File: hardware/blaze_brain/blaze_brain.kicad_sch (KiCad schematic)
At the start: 26 parts, among them J1 Conn_01x02, J2 Conn_01x02, J3 Conn_01x30, J4 Micro_SD_Card, J5 Conn_01x03_Pin, Q1 DMG2305UX, Q2 FDN340P, U1 AZ1117-5.0, U2 AZ1117-3.3, U3 Teensy4.0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

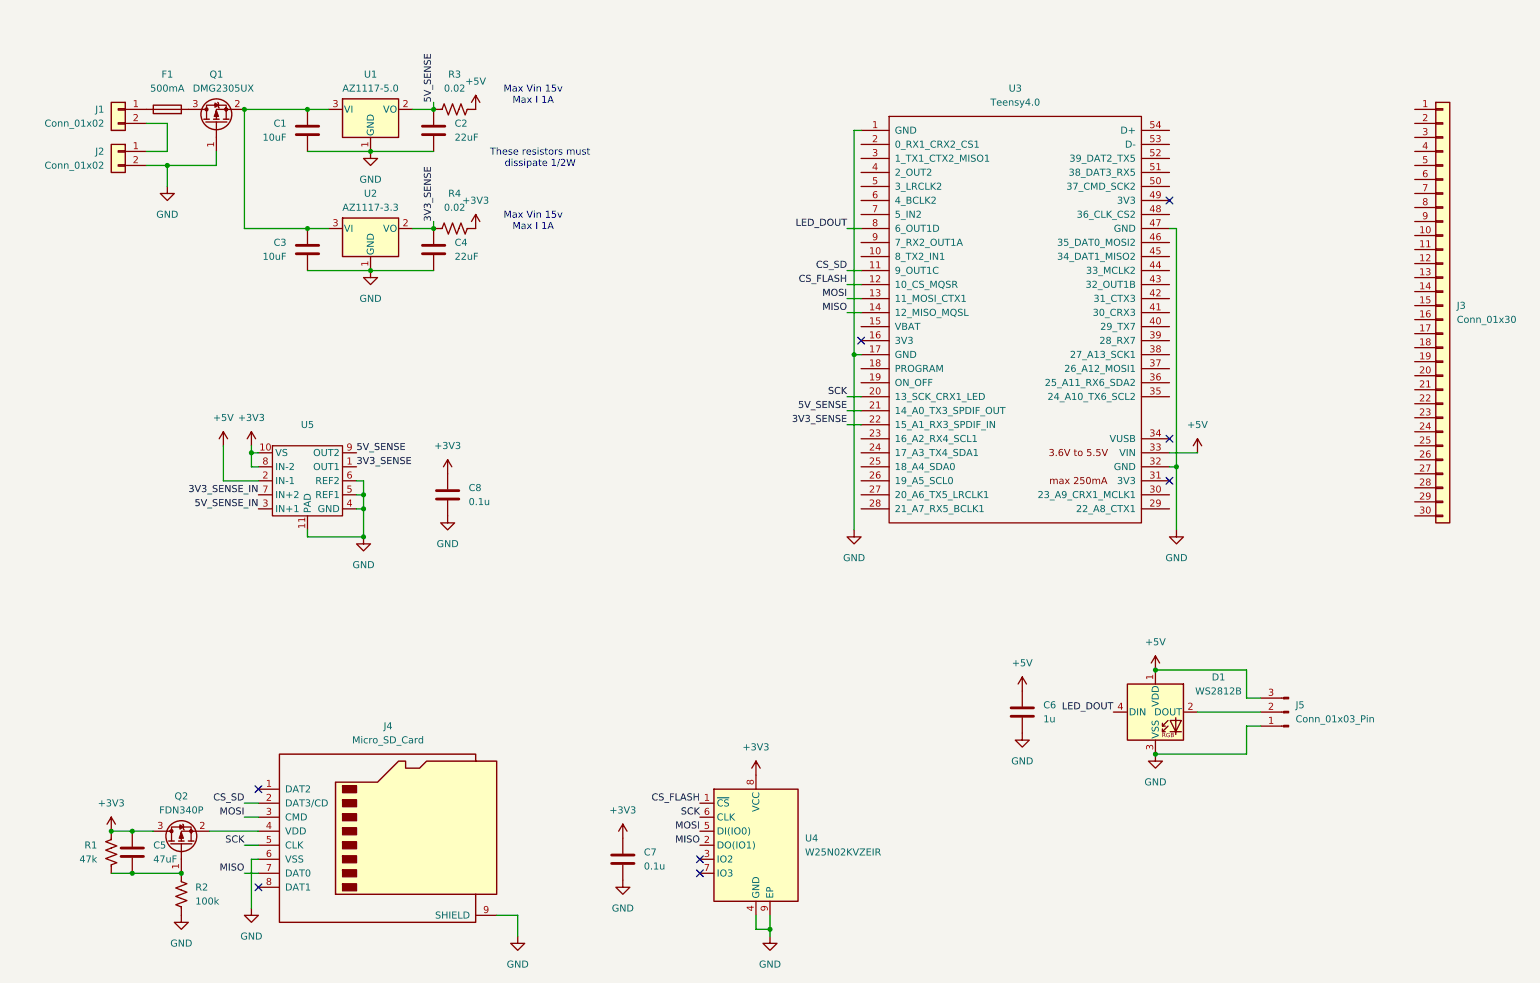
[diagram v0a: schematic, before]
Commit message: Moved main power function to power management
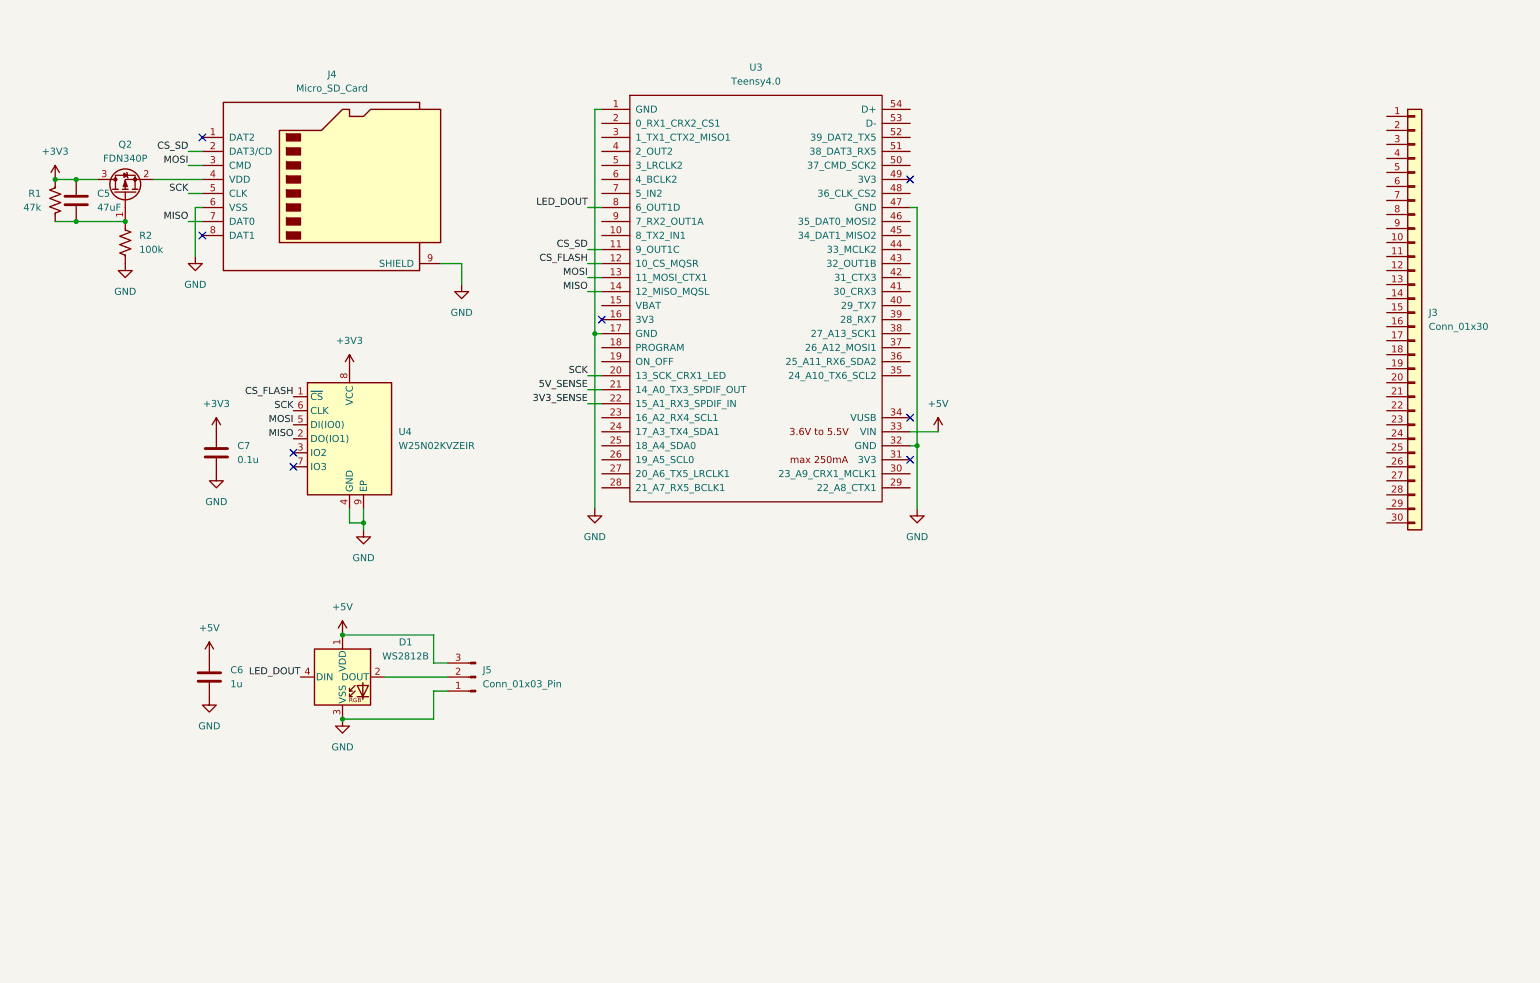
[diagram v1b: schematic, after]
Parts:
- removed C1, C3: 10uF, symbol Device:C
- removed C2, C4: 22uF, symbol Device:C
- removed C8: 0.1u, symbol Device:C
- removed F1: 500mA, symbol Device:Fuse
- removed J1, J2: Conn_01x02, symbol Connector_Generic:Conn_01x02
- removed Q1: DMG2305UX, Package_TO_SOT_SMD:SOT-23, symbol Transistor_FET:DMG2301L
- removed R3, R4: 0.02, symbol Device:R_US
- removed U1: AZ1117-5.0, Package_TO_SOT_SMD:SOT-223-3_TabPin2, symbol Regulator_Linear:AZ1117-5.0
- removed U2: AZ1117-3.3, Package_TO_SOT_SMD:SOT-223-3_TabPin2, symbol Regulator_Linear:AZ1117-5.0
- removed U5: ~, symbol Blaze_Lib:INA2181
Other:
- note removed: "Max Vin 15v Max I 1A"
- note removed: "These resistors must dissipate 1/2W"
- moved on the sheet: C5, C6, C7, D1, J3, J4, J5, Q2, R1, R2, U3, U4

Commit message: Created blaze sense, updated brain
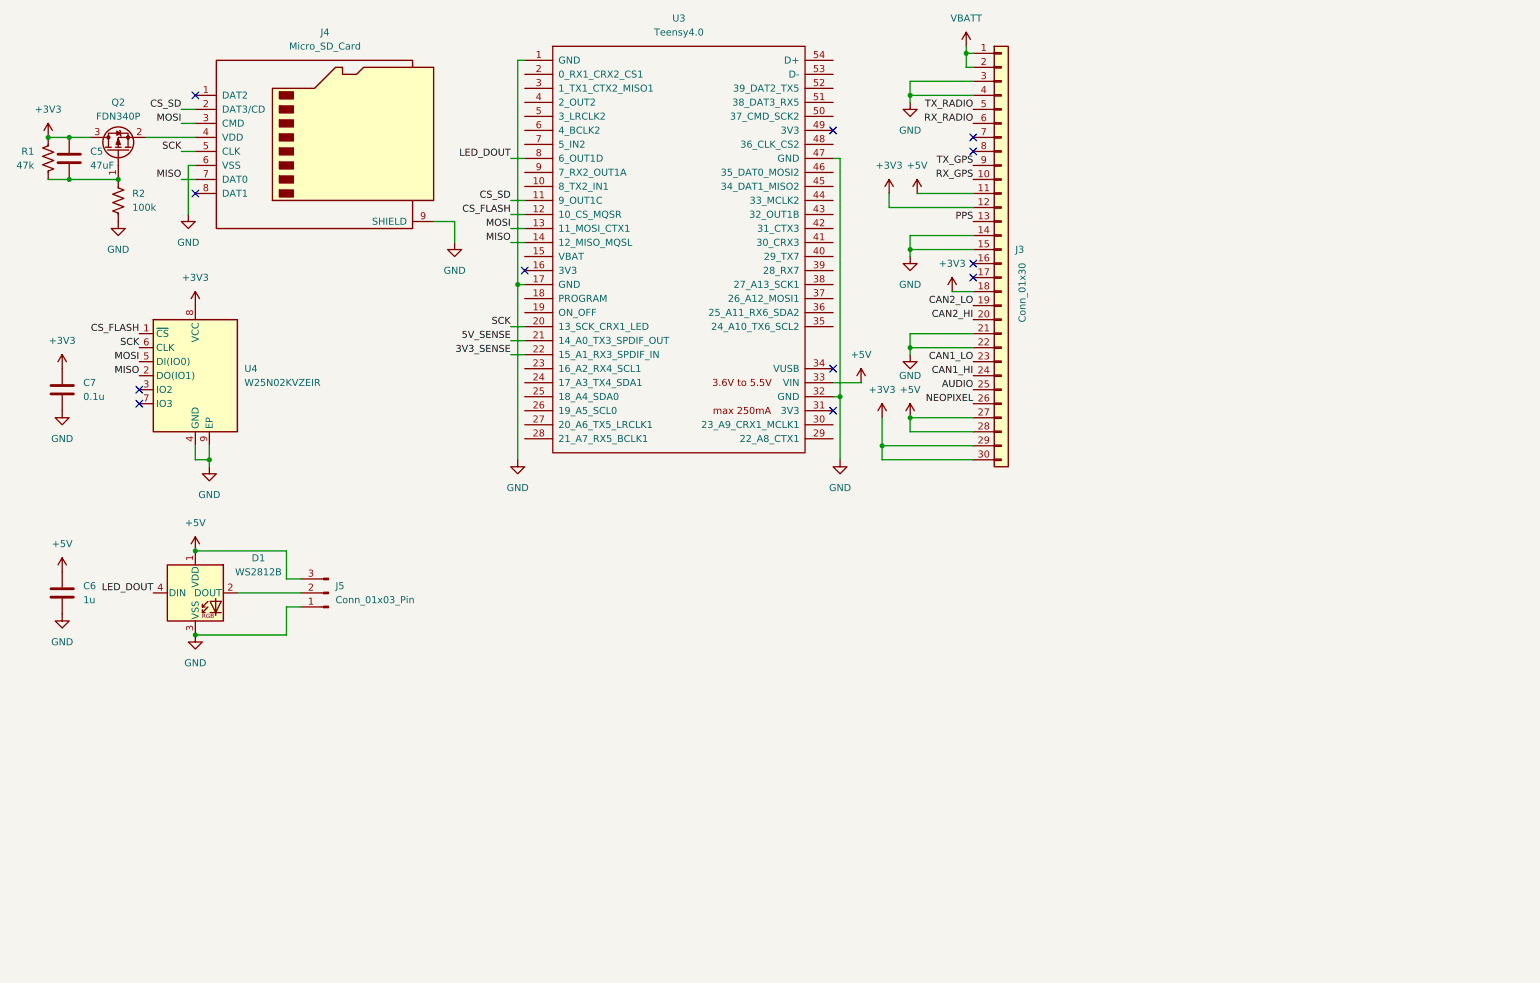
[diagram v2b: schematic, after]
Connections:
- net +3V3: now also J3.12 (Pin_12), J3.18 (Pin_18), J3.29 (Pin_29), J3.30 (Pin_30)
- net +5V: now also J3.11 (Pin_11), J3.27 (Pin_27), J3.28 (Pin_28)
- net GND: now also J3.14 (Pin_14), J3.15 (Pin_15), J3.21 (Pin_21), J3.22 (Pin_22), J3.3 (Pin_3), J3.4 (Pin_4)
- net VBATT: now reaches J3.1 (Pin_1)
- net VBATT: now also J3.2 (Pin_2)
- net RX_GPS: now reaches J3.10 (Pin_10)
- net PPS: now reaches J3.13 (Pin_13)
- net CAN2_LO: now reaches J3.19 (Pin_19)
- net CAN2_HI: now reaches J3.20 (Pin_20)
- net CAN1_LO: now reaches J3.23 (Pin_23)
- net CAN1_HI: now reaches J3.24 (Pin_24)
- net AUDIO: now reaches J3.25 (Pin_25)
- net NEOPIXEL: now reaches J3.26 (Pin_26)
- net TX_RADIO: now reaches J3.5 (Pin_5)
- net RX_RADIO: now reaches J3.6 (Pin_6)
- net TX_GPS: now reaches J3.9 (Pin_9)
- no-connect marks 8 -> 12
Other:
- company: (none) -> UCSC Rocket Team
- moved on the sheet: C5, C6, C7, D1, J3, J4, J5, Q2, R1, R2, U3, U4

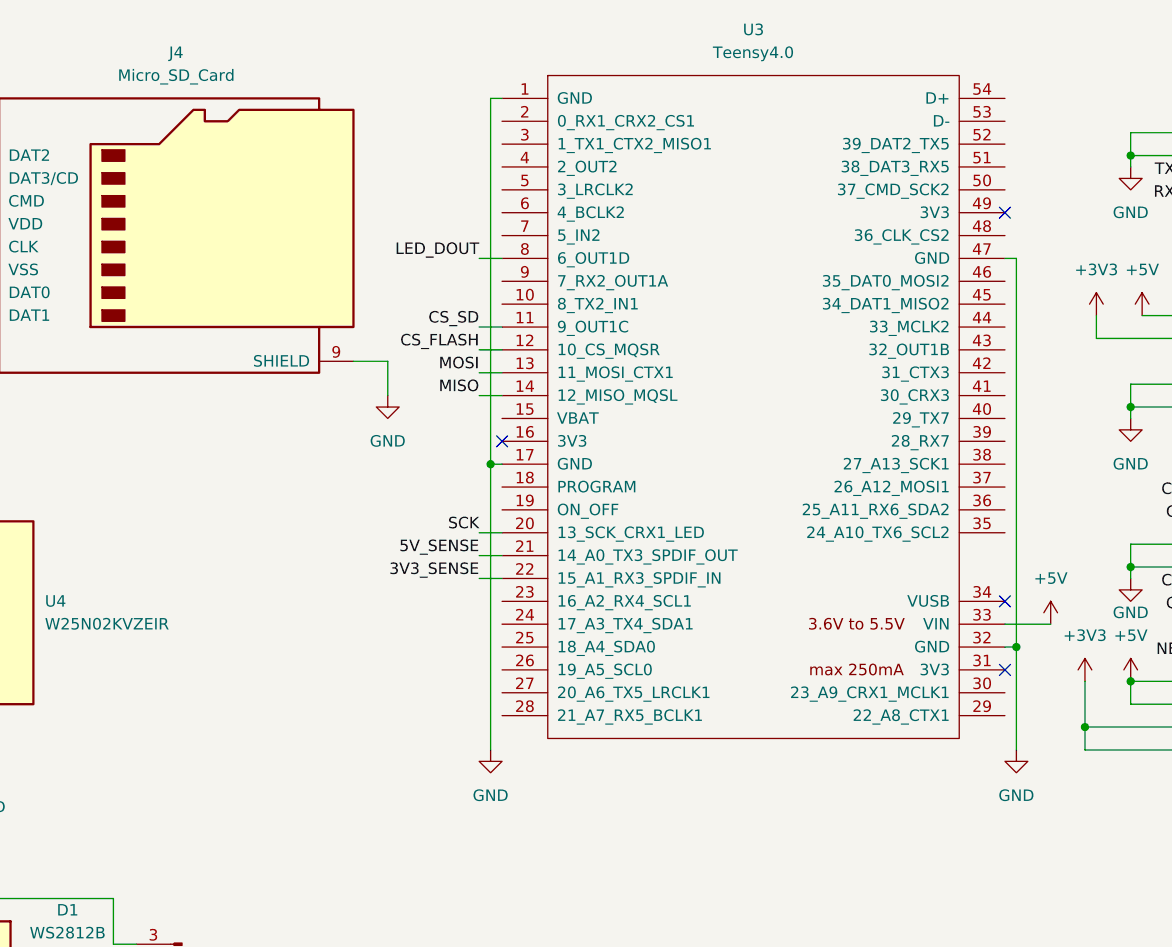
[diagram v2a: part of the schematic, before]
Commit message: Created blaze io
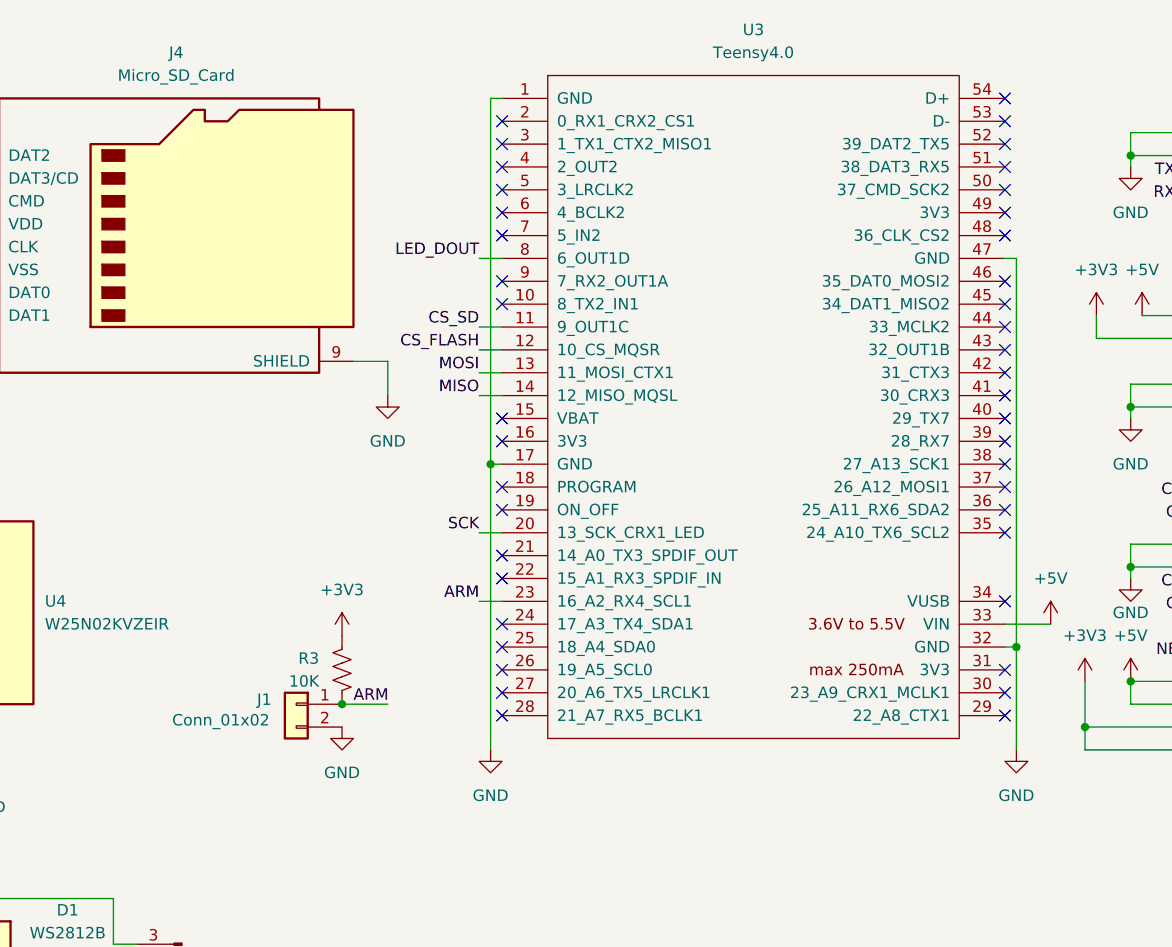
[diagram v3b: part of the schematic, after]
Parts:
- added J1: Conn_01x02, symbol Connector_Generic:Conn_01x02
- added R3: 10K, symbol Device:R_US
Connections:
- net +3V3: now also R3.1
- net GND: now also J1.2 (Pin_2)
- net ARM: now reaches U3.23 (16_A2_RX4_SCL1)
- net ARM: now also J1.1 (Pin_1), R3.2
- net 3V3_SENSE: no longer names the net of U3.22 (15_A1_RX3_SPDIF_IN)
- net 5V_SENSE: no longer names the net of U3.21 (14_A0_TX3_SPDIF_OUT)
- no-connect marks 12 -> 50

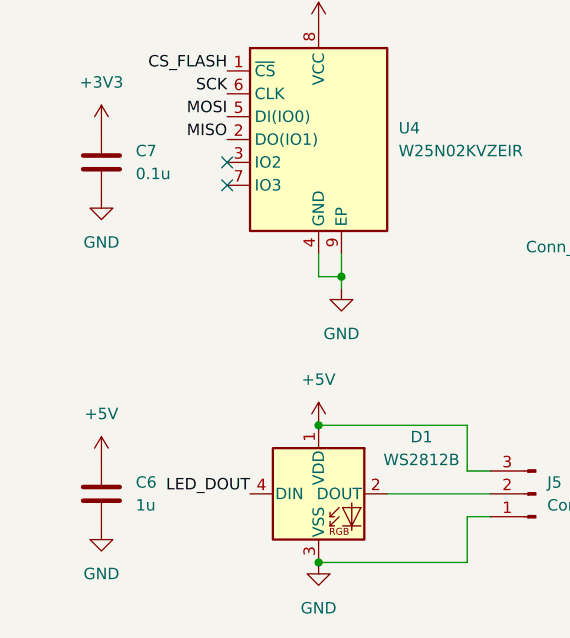
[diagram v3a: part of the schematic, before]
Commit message: Connected IO, wrote docs
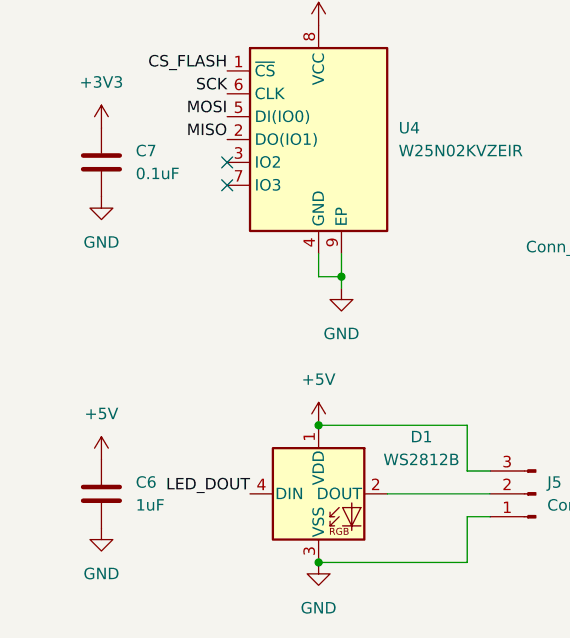
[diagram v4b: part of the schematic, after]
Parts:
- C6: value 1u -> 1uF
- C7: value 0.1u -> 0.1uF
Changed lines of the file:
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@@
 			)
 		)
-		(property "Value" "0.1u"
+		(property "Value" "0.1uF"
 			(at 25.4 85.0899 0)
 			(effects
@@
 			)
 		)
-		(property "Value" "1u"
+		(property "Value" "1uF"
 			(at 25.4 121.9199 0)
 			(effects
